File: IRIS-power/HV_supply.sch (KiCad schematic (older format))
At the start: 17 parts

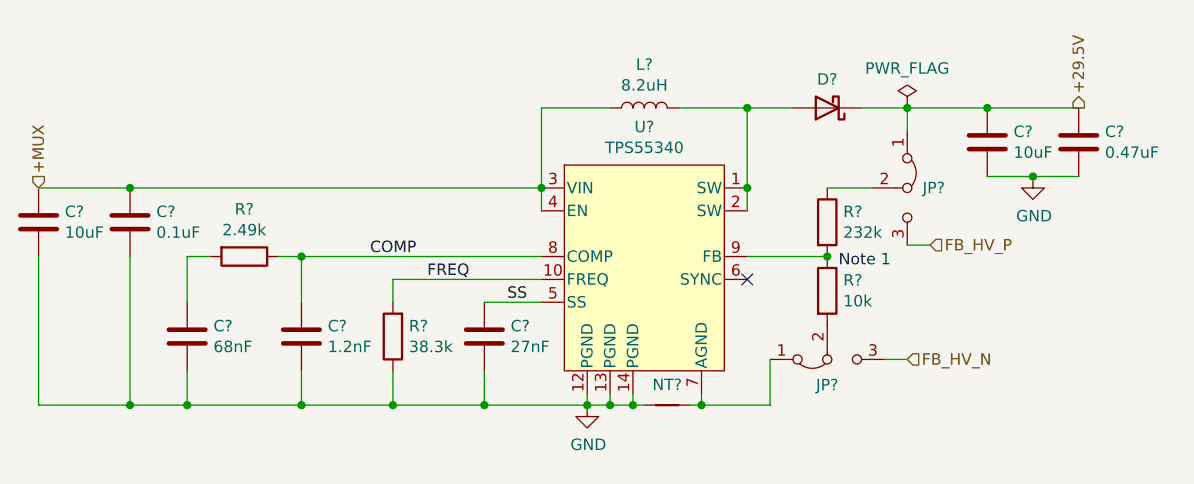
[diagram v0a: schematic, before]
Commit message: Finalized power board V2 schematic, preparing to layout
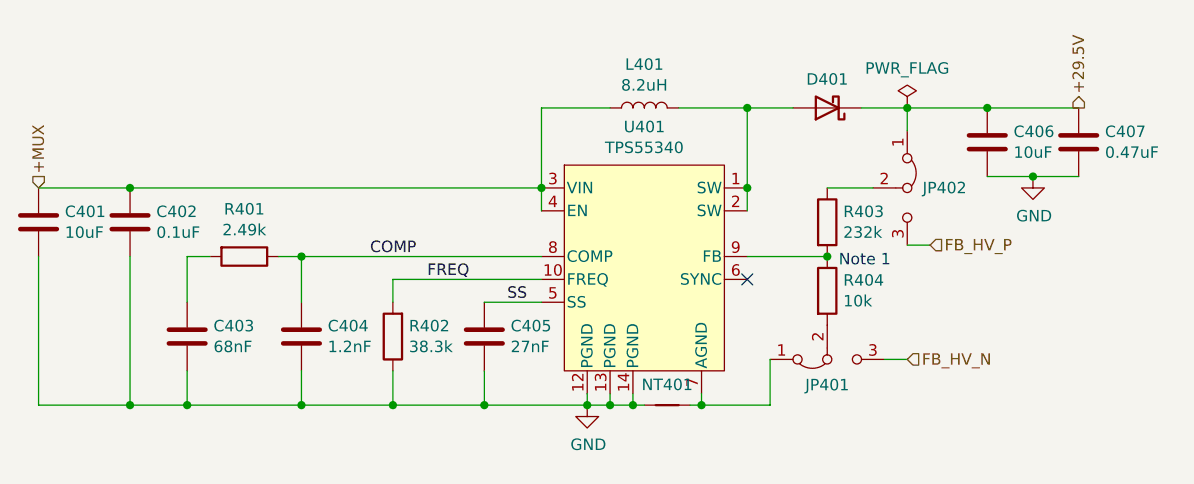
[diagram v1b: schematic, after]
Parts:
- C401, C406: renamed from C?; footprint Capacitor_SMD:C_1206_3216Metric -> Capacitor_SMD:C_0603_1608Metric
- C402, C403, C404, C407: renamed from C?; footprint (none) -> Capacitor_SMD:C_0603_1608Metric
- JP401, JP402: renamed from JP?; footprint (none) -> Connector_PinHeader_2.54mm:PinHeader_1x03_P2.54mm_Vertical
- L401: renamed from L?; footprint (none) -> star-common-lib:VLS6045AF
- NT401: renamed from NT?; footprint (none) -> NetTie:NetTie-2_SMD_Pad0.5mm
- R401: renamed from R?; footprint (none) -> Resistor_SMD:R_0603_1608Metric
- U401: renamed from U?; footprint (none) -> star-common-lib:TPS55340
- gave numbers to parts that had none: 5
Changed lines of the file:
@@
 $Descr A4 11693 8268
 encoding utf-8
-Sheet 5 9
+Sheet 4 8
 Title ""
 Date ""
@@
 P 5000 4250
 AR Path="/5F441757" Ref="R?"  Part="1"
-AR Path="/5F41AE09/5F441757" Ref="R?"  Part="1"
-F 0 "R?" H 4930 4204 50  0000 R CNN
+AR Path="/5F41AE09/5F441757" Ref="R402"  Part="1"
+F 0 "R402" H 4930 4204 50  0000 R CNN
 F 1 "38.3k" H 4930 4295 50  0000 R CNN
 F 2 "Resistor_SMD:R_0603_1608Metric" V 4930 4250 50  0001 C CNN
@@
 P 5400 4250
 AR Path="/5F44175D" Ref="C?"  Part="1"
-AR Path="/5F41AE09/5F44175D" Ref="C?"  Part="1"
-F 0 "C?" H 5515 4296 50  0000 L CNN
+AR Path="/5F41AE09/5F44175D" Ref="C405"  Part="1"
+F 0 "C405" H 5515 4296 50  0000 L CNN
 F 1 "27nF" H 5515 4205 50  0000 L CNN
 F 2 "Capacitor_SMD:C_0603_1608Metric" H 5438 4100 50  0001 C CNN
@@
 P 3450 3750
 AR Path="/5F441768" Ref="C?"  Part="1"
-AR Path="/5F41AE09/5F441768" Ref="C?"  Part="1"
-F 0 "C?" H 3565 3796 50  0000 L CNN
+AR Path="/5F41AE09/5F441768" Ref="C401"  Part="1"
+F 0 "C401" H 3565 3796 50  0000 L CNN
 F 1 "10uF" H 3565 3705 50  0000 L CNN
-F 2 "Capacitor_SMD:C_1206_3216Metric" H 3488 3600 50  0001 C CNN
+F 2 "Capacitor_SMD:C_0603_1608Metric" H 3488 3600 50  0001 C CNN
 F 3 "~" H 3450 3750 50  0001 C CNN
 F 4 "X5R, 16V" H 3450 3750 50  0001 C CNN "Notes"
@@
 P 6900 3750
 AR Path="/5F44176E" Ref="R?"  Part="1"
-AR Path="/5F41AE09/5F44176E" Ref="R?"  Part="1"
-F 0 "R?" H 6970 3796 50  0000 L CNN
+AR Path="/5F41AE09/5F44176E" Ref="R403"  Part="1"
+F 0 "R403" H 6970 3796 50  0000 L CNN
 F 1 "232k" H 6970 3705 50  0000 L CNN
 F 2 "Resistor_SMD:R_0603_1608Metric" V 6830 3750 50  0001 C CNN
@@
 P 6900 4050
 AR Path="/5F441774" Ref="R?"  Part="1"
-AR Path="/5F41AE09/5F441774" Ref="R?"  Part="1"
-F 0 "R?" H 6970 4096 50  0000 L CNN
+AR Path="/5F41AE09/5F441774" Ref="R404"  Part="1"
+F 0 "R404" H 6970 4096 50  0000 L CNN
 F 1 "10k" H 6970 4005 50  0000 L CNN
 F 2 "Resistor_SMD:R_0603_1608Metric" V 6830 4050 50  0001 C CNN
@@
 P 7600 3400
 AR Path="/5F44177A" Ref="C?"  Part="1"
-AR Path="/5F41AE09/5F44177A" Ref="C?"  Part="1"
-F 0 "C?" H 7715 3446 50  0000 L CNN
+AR Path="/5F41AE09/5F44177A" Ref="C406"  Part="1"
+F 0 "C406" H 7715 3446 50  0000 L CNN
 F 1 "10uF" H 7715 3355 50  0000 L CNN
-F 2 "Capacitor_SMD:C_1206_3216Metric" H 7638 3250 50  0001 C CNN
+F 2 "Capacitor_SMD:C_0603_1608Metric" H 7638 3250 50  0001 C CNN
 F 3 "1276-3387-1-ND" H 7600 3400 50  0001 C CNN
 	1    7600 3400
@@
 P 5850 4550
 AR Path="/5F441780" Ref="#PWR?"  Part="1"
-AR Path="/5F41AE09/5F441780" Ref="#PWR?"  Part="1"
-F 0 "#PWR?" H 5850 4300 50  0001 C CNN
+AR Path="/5F41AE09/5F441780" Ref="#PWR0401"  Part="1"
+F 0 "#PWR0401" H 5850 4300 50  0001 C CNN
 F 1 "GND" H 5855 4377 50  0000 C CNN
 F 2 "" H 5850 4550 50  0001 C CNN
@@
 P 7250 3250
 AR Path="/5F441786" Ref="#FLG?"  Part="1"
-AR Path="/5F41AE09/5F441786" Ref="#FLG?"  Part="1"
-F 0 "#FLG?" H 7250 3325 50  0001 C CNN
+AR Path="/5F41AE09/5F441786" Ref="#FLG0401"  Part="1"
+F 0 "#FLG0401" H 7250 3325 50  0001 C CNN
 F 1 "PWR_FLAG" H 7250 3423 50  0000 C CNN
 F 2 "" H 7250 3250 50  0001 C CNN
@@
 P 6100 3950
 AR Path="/5F44178F" Ref="U?"  Part="1"
-AR Path="/5F41AE09/5F44178F" Ref="U?"  Part="1"
-F 0 "U?" H 6100 4567 50  0000 C CNN
+AR Path="/5F41AE09/5F44178F" Ref="U401"  Part="1"
+F 0 "U401" H 6100 4567 50  0000 C CNN
 F 1 "TPS55340" H 6100 4476 50  0000 C CNN
-F 2 "" H 6100 3700 50  0001 L CNN
+F 2 "star-common-lib:TPS55340" H 6100 3700 50  0001 L CNN
 F 3 "" H 5850 3600 50  0001 C CNN
 	1    6100 3950
@@
 P 6100 3250
 AR Path="/5F4417A5" Ref="L?"  Part="1"
-AR Path="/5F41AE09/5F4417A5" Ref="L?"  Part="1"
-F 0 "L?" V 6290 3250 50  0000 C CNN
+AR Path="/5F41AE09/5F4417A5" Ref="L401"  Part="1"
+F 0 "L401" V 6290 3250 50  0000 C CNN
 F 1 "8.2uH" V 6199 3250 50  0000 C CNN
-F 2 "" H 6100 3250 50  0001 C CNN
+F 2 "star-common-lib:VLS6045AF" H 6100 3250 50  0001 C CNN
 F 3 "https://product.tdk.com/info/en/catalog/datasheets/inductor_commercial_power_vls6045af_en.pdf" H 6100 3250 50  0001 C CNN
 F 4 "445-VLS6045AF-8R2MCT-ND" H 6100 3250 50  0001 C CNN "Digikey PN"
@@
 P 6900 3250
 AR Path="/5F4417AE" Ref="D?"  Part="1"
-AR Path="/5F41AE09/5F4417AE" Ref="D?"  Part="1"
-F 0 "D?" H 6900 3125 50  0000 C CNN
+AR Path="/5F41AE09/5F4417AE" Ref="D401"  Part="1"
+F 0 "D401" H 6900 3125 50  0000 C CNN
 F 1 "D_Schottky" H 6900 3124 50  0001 C CNN
 F 2 "Diode_SMD:D_SMA_Handsoldering" H 6900 3250 50  0001 C CNN
@@
 P 4100 4250
 AR Path="/5F4417B4" Ref="C?"  Part="1"
-AR Path="/5F41AE09/5F4417B4" Ref="C?"  Part="1"
-F 0 "C?" H 4215 4296 50  0000 L CNN
+AR Path="/5F41AE09/5F4417B4" Ref="C403"  Part="1"
+F 0 "C403" H 4215 4296 50  0000 L CNN
 F 1 "68nF" H 4215 4205 50  0000 L CNN
-F 2 "" H 4138 4100 50  0001 C CNN
+F 2 "Capacitor_SMD:C_0603_1608Metric" H 4138 4100 50  0001 C CNN
 F 3 "~" H 4100 4250 50  0001 C CNN
 	1    4100 4250
@@
 P 4600 4250
 AR Path="/5F4417BA" Ref="C?"  Part="1"
-AR Path="/5F41AE09/5F4417BA" Ref="C?"  Part="1"
-F 0 "C?" H 4715 4296 50  0000 L CNN
+AR Path="/5F41AE09/5F4417BA" Ref="C404"  Part="1"
+F 0 "C404" H 4715 4296 50  0000 L CNN
 F 1 "1.2nF" H 4715 4205 50  0000 L CNN
-F 2 "" H 4638 4100 50  0001 C CNN
+F 2 "Capacitor_SMD:C_0603_1608Metric" H 4638 4100 50  0001 C CNN
 F 3 "~" H 4600 4250 50  0001 C CNN
 	1    4600 4250
@@
 P 4350 3900
 AR Path="/5F4417C0" Ref="R?"  Part="1"
-AR Path="/5F41AE09/5F4417C0" Ref="R?"  Part="1"
-F 0 "R?" V 4143 3900 50  0000 C CNN
+AR Path="/5F41AE09/5F4417C0" Ref="R401"  Part="1"
+F 0 "R401" V 4143 3900 50  0000 C CNN
 F 1 "2.49k" V 4234 3900 50  0000 C CNN
-F 2 "" V 4280 3900 50  0001 C CNN
+F 2 "Resistor_SMD:R_0603_1608Metric" V 4280 3900 50  0001 C CNN
 F 3 "~" H 4350 3900 50  0001 C CNN
 	1    4350 3900
@@
 P 7250 3600
 AR Path="/5F4417C6" Ref="JP?"  Part="1"
-AR Path="/5F41AE09/5F4417C6" Ref="JP?"  Part="1"
-F 0 "JP?" V 7250 3667 50  0000 L CNN
+AR Path="/5F41AE09/5F4417C6" Ref="JP402"  Part="1"
+F 0 "JP402" V 7250 3667 50  0000 L CNN
 F 1 "Jumper_3_Bridged12" V 7295 3667 50  0001 L CNN
-F 2 "" H 7250 3600 50  0001 C CNN
+F 2 "Connector_PinHeader_2.54mm:PinHeader_1x03_P2.54mm_Vertical" H 7250 3600 50  0001 C CNN
 F 3 "~" H 7250 3600 50  0001 C CNN
 	1    7250 3600
@@
 P 6900 4350
 AR Path="/5F4417CE" Ref="JP?"  Part="1"
-AR Path="/5F41AE09/5F4417CE" Ref="JP?"  Part="1"
-F 0 "JP?" H 6900 4462 50  0000 C CNN
+AR Path="/5F41AE09/5F4417CE" Ref="JP401"  Part="1"
+F 0 "JP401" H 6900 4462 50  0000 C CNN
 F 1 "Jumper_3_Bridged12" H 6900 4552 50  0001 C CNN
-F 2 "" H 6900 4350 50  0001 C CNN
+F 2 "Connector_PinHeader_2.54mm:PinHeader_1x03_P2.54mm_Vertical" H 6900 4350 50  0001 C CNN
 F 3 "~" H 6900 4350 50  0001 C CNN
 	1    6900 4350
@@
 P 6200 4550
 AR Path="/5F4417D4" Ref="NT?"  Part="1"
-AR Path="/5F41AE09/5F4417D4" Ref="NT?"  Part="1"
-F 0 "NT?" H 6200 4639 50  0000 C CNN
+AR Path="/5F41AE09/5F4417D4" Ref="NT401"  Part="1"
+F 0 "NT401" H 6200 4639 50  0000 C CNN
 F 1 "Net-Tie_2" H 6200 4640 50  0001 C CNN
-F 2 "" H 6200 4550 50  0001 C CNN
+F 2 "NetTie:NetTie-2_SMD_Pad0.5mm" H 6200 4550 50  0001 C CNN
 F 3 "~" H 6200 4550 50  0001 C CNN
 	1    6200 4550
@@
 P 7800 3550
 AR Path="/5F4417FB" Ref="#PWR?"  Part="1"
-AR Path="/5F41AE09/5F4417FB" Ref="#PWR?"  Part="1"
-F 0 "#PWR?" H 7800 3300 50  0001 C CNN
+AR Path="/5F41AE09/5F4417FB" Ref="#PWR0402"  Part="1"
+F 0 "#PWR0402" H 7800 3300 50  0001 C CNN
 F 1 "GND" H 7805 3377 50  0000 C CNN
 F 2 "" H 7800 3550 50  0001 C CNN
@@
 P 3850 3750
 AR Path="/5F44180C" Ref="C?"  Part="1"
-AR Path="/5F41AE09/5F44180C" Ref="C?"  Part="1"
-F 0 "C?" H 3965 3796 50  0000 L CNN
+AR Path="/5F41AE09/5F44180C" Ref="C402"  Part="1"
+F 0 "C402" H 3965 3796 50  0000 L CNN
 F 1 "0.1uF" H 3965 3705 50  0000 L CNN
-F 2 "" H 3888 3600 50  0001 C CNN
+F 2 "Capacitor_SMD:C_0603_1608Metric" H 3888 3600 50  0001 C CNN
 F 3 "~" H 3850 3750 50  0001 C CNN
 	1    3850 3750
@@
 P 8000 3400
 AR Path="/5F441812" Ref="C?"  Part="1"
-AR Path="/5F41AE09/5F441812" Ref="C?"  Part="1"
-F 0 "C?" H 8115 3446 50  0000 L CNN
+AR Path="/5F41AE09/5F441812" Ref="C407"  Part="1"
+F 0 "C407" H 8115 3446 50  0000 L CNN
 F 1 "0.47uF" H 8115 3355 50  0000 L CNN
-F 2 "" H 8038 3250 50  0001 C CNN
+F 2 "Capacitor_SMD:C_0603_1608Metric" H 8038 3250 50  0001 C CNN
 F 3 "~" H 8000 3400 50  0001 C CNN
 	1    8000 3400

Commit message: Updated layout
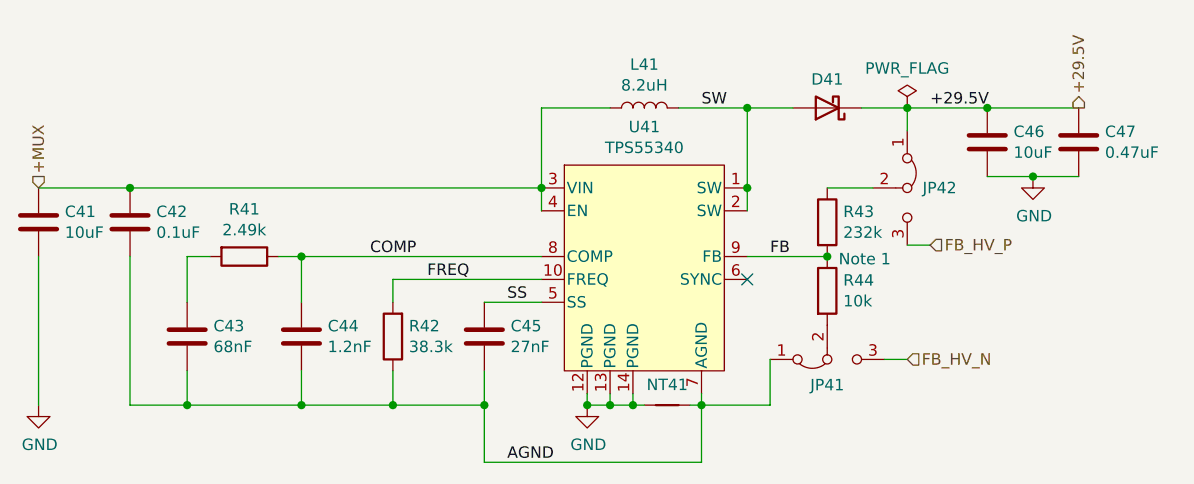
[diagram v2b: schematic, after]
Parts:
- C46: renamed from C406; footprint Capacitor_SMD:C_0603_1608Metric -> Capacitor_SMD:C_0805_2012Metric
- renumbered C401 to C41, C402 to C42, C403 to C43, C404 to C44, C405 to C45, C407 to C47, D401 to D41, JP401 to JP41, JP402 to JP42, L401 to L41, NT401 to NT41, R401 to R41, R402 to R42, R403 to R43, R404 to R44, U401 to U41
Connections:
- net GND: no longer C42.2, C43.2, C44.2, C45.2, R42.1
- net FB: now reaches R43.2, R44.1, U41.9 (FB)
- net SW: now reaches D41.2 (A), L41.2, U41.1 (SW), U41.2 (SW)
- net AGND: now reaches JP41.1 (A), NT41.2, U41.7 (AGND)
- net AGND: now also C42.2, C43.2, C44.2, C45.2, R42.1
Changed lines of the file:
@@
 	6550 3600 6550 3700
 Connection ~ 6550 3600
-Connection ~ 5400 4550
-Wire Wire Line
-	5400 4550 5850 4550
 Connection ~ 5650 3600
 Connection ~ 3850 3600
@@
 P 5000 4250
 AR Path="/5F441757" Ref="R?"  Part="1"
-AR Path="/5F41AE09/5F441757" Ref="R402"  Part="1"
-F 0 "R402" H 4930 4204 50  0000 R CNN
+AR Path="/5F41AE09/5F441757" Ref="R42"  Part="1"
+F 0 "R42" H 4930 4204 50  0000 R CNN
 F 1 "38.3k" H 4930 4295 50  0000 R CNN
 F 2 "Resistor_SMD:R_0603_1608Metric" V 4930 4250 50  0001 C CNN
@@
 P 5400 4250
 AR Path="/5F44175D" Ref="C?"  Part="1"
-AR Path="/5F41AE09/5F44175D" Ref="C405"  Part="1"
-F 0 "C405" H 5515 4296 50  0000 L CNN
+AR Path="/5F41AE09/5F44175D" Ref="C45"  Part="1"
+F 0 "C45" H 5515 4296 50  0000 L CNN
 F 1 "27nF" H 5515 4205 50  0000 L CNN
 F 2 "Capacitor_SMD:C_0603_1608Metric" H 5438 4100 50  0001 C CNN
@@
 P 3450 3750
 AR Path="/5F441768" Ref="C?"  Part="1"
-AR Path="/5F41AE09/5F441768" Ref="C401"  Part="1"
-F 0 "C401" H 3565 3796 50  0000 L CNN
+AR Path="/5F41AE09/5F441768" Ref="C41"  Part="1"
+F 0 "C41" H 3565 3796 50  0000 L CNN
 F 1 "10uF" H 3565 3705 50  0000 L CNN
 F 2 "Capacitor_SMD:C_0603_1608Metric" H 3488 3600 50  0001 C CNN
@@
 P 6900 3750
 AR Path="/5F44176E" Ref="R?"  Part="1"
-AR Path="/5F41AE09/5F44176E" Ref="R403"  Part="1"
-F 0 "R403" H 6970 3796 50  0000 L CNN
+AR Path="/5F41AE09/5F44176E" Ref="R43"  Part="1"
+F 0 "R43" H 6970 3796 50  0000 L CNN
 F 1 "232k" H 6970 3705 50  0000 L CNN
 F 2 "Resistor_SMD:R_0603_1608Metric" V 6830 3750 50  0001 C CNN
@@
 P 6900 4050
 AR Path="/5F441774" Ref="R?"  Part="1"
-AR Path="/5F41AE09/5F441774" Ref="R404"  Part="1"
-F 0 "R404" H 6970 4096 50  0000 L CNN
+AR Path="/5F41AE09/5F441774" Ref="R44"  Part="1"
+F 0 "R44" H 6970 4096 50  0000 L CNN
 F 1 "10k" H 6970 4005 50  0000 L CNN
 F 2 "Resistor_SMD:R_0603_1608Metric" V 6830 4050 50  0001 C CNN
@@
 P 7600 3400
 AR Path="/5F44177A" Ref="C?"  Part="1"
-AR Path="/5F41AE09/5F44177A" Ref="C406"  Part="1"
-F 0 "C406" H 7715 3446 50  0000 L CNN
+AR Path="/5F41AE09/5F44177A" Ref="C46"  Part="1"
+F 0 "C46" H 7715 3446 50  0000 L CNN
 F 1 "10uF" H 7715 3355 50  0000 L CNN
-F 2 "Capacitor_SMD:C_0603_1608Metric" H 7638 3250 50  0001 C CNN
+F 2 "Capacitor_SMD:C_0805_2012Metric" H 7638 3250 50  0001 C CNN
 F 3 "1276-3387-1-ND" H 7600 3400 50  0001 C CNN
 	1    7600 3400
@@
 P 5850 4550
 AR Path="/5F441780" Ref="#PWR?"  Part="1"
-AR Path="/5F41AE09/5F441780" Ref="#PWR0401"  Part="1"
-F 0 "#PWR0401" H 5850 4300 50  0001 C CNN
+AR Path="/5F41AE09/5F441780" Ref="#PWR042"  Part="1"
+F 0 "#PWR042" H 5850 4300 50  0001 C CNN
 F 1 "GND" H 5855 4377 50  0000 C CNN
 F 2 "" H 5850 4550 50  0001 C CNN
@@
 P 7250 3250
 AR Path="/5F441786" Ref="#FLG?"  Part="1"
-AR Path="/5F41AE09/5F441786" Ref="#FLG0401"  Part="1"
-F 0 "#FLG0401" H 7250 3325 50  0001 C CNN
+AR Path="/5F41AE09/5F441786" Ref="#FLG041"  Part="1"
+F 0 "#FLG041" H 7250 3325 50  0001 C CNN
 F 1 "PWR_FLAG" H 7250 3423 50  0000 C CNN
 F 2 "" H 7250 3250 50  0001 C CNN
@@
 P 6100 3950
 AR Path="/5F44178F" Ref="U?"  Part="1"
-AR Path="/5F41AE09/5F44178F" Ref="U401"  Part="1"
-F 0 "U401" H 6100 4567 50  0000 C CNN
+AR Path="/5F41AE09/5F44178F" Ref="U41"  Part="1"
+F 0 "U41" H 6100 4567 50  0000 C CNN
 F 1 "TPS55340" H 6100 4476 50  0000 C CNN
 F 2 "star-common-lib:TPS55340" H 6100 3700 50  0001 L CNN
@@
 P 6100 3250
 AR Path="/5F4417A5" Ref="L?"  Part="1"
-AR Path="/5F41AE09/5F4417A5" Ref="L401"  Part="1"
-F 0 "L401" V 6290 3250 50  0000 C CNN
+AR Path="/5F41AE09/5F4417A5" Ref="L41"  Part="1"
+F 0 "L41" V 6290 3250 50  0000 C CNN
 F 1 "8.2uH" V 6199 3250 50  0000 C CNN
 F 2 "star-common-lib:VLS6045AF" H 6100 3250 50  0001 C CNN
@@
 P 6900 3250
 AR Path="/5F4417AE" Ref="D?"  Part="1"
-AR Path="/5F41AE09/5F4417AE" Ref="D401"  Part="1"
-F 0 "D401" H 6900 3125 50  0000 C CNN
+AR Path="/5F41AE09/5F4417AE" Ref="D41"  Part="1"
+F 0 "D41" H 6900 3125 50  0000 C CNN
 F 1 "D_Schottky" H 6900 3124 50  0001 C CNN
 F 2 "Diode_SMD:D_SMA_Handsoldering" H 6900 3250 50  0001 C CNN
@@
 P 4100 4250
 AR Path="/5F4417B4" Ref="C?"  Part="1"
-AR Path="/5F41AE09/5F4417B4" Ref="C403"  Part="1"
-F 0 "C403" H 4215 4296 50  0000 L CNN
+AR Path="/5F41AE09/5F4417B4" Ref="C43"  Part="1"
+F 0 "C43" H 4215 4296 50  0000 L CNN
 F 1 "68nF" H 4215 4205 50  0000 L CNN
 F 2 "Capacitor_SMD:C_0603_1608Metric" H 4138 4100 50  0001 C CNN
@@
 P 4600 4250
 AR Path="/5F4417BA" Ref="C?"  Part="1"
-AR Path="/5F41AE09/5F4417BA" Ref="C404"  Part="1"
-F 0 "C404" H 4715 4296 50  0000 L CNN
+AR Path="/5F41AE09/5F4417BA" Ref="C44"  Part="1"
+F 0 "C44" H 4715 4296 50  0000 L CNN
 F 1 "1.2nF" H 4715 4205 50  0000 L CNN
 F 2 "Capacitor_SMD:C_0603_1608Metric" H 4638 4100 50  0001 C CNN
@@
 P 4350 3900
 AR Path="/5F4417C0" Ref="R?"  Part="1"
-AR Path="/5F41AE09/5F4417C0" Ref="R401"  Part="1"
-F 0 "R401" V 4143 3900 50  0000 C CNN
+AR Path="/5F41AE09/5F4417C0" Ref="R41"  Part="1"
+F 0 "R41" V 4143 3900 50  0000 C CNN
 F 1 "2.49k" V 4234 3900 50  0000 C CNN
 F 2 "Resistor_SMD:R_0603_1608Metric" V 4280 3900 50  0001 C CNN
@@
 P 7250 3600
 AR Path="/5F4417C6" Ref="JP?"  Part="1"
-AR Path="/5F41AE09/5F4417C6" Ref="JP402"  Part="1"
-F 0 "JP402" V 7250 3667 50  0000 L CNN
+AR Path="/5F41AE09/5F4417C6" Ref="JP42"  Part="1"
+F 0 "JP42" V 7250 3667 50  0000 L CNN
 F 1 "Jumper_3_Bridged12" V 7295 3667 50  0001 L CNN
 F 2 "Connector_PinHeader_2.54mm:PinHeader_1x03_P2.54mm_Vertical" H 7250 3600 50  0001 C CNN
@@
 P 6900 4350
 AR Path="/5F4417CE" Ref="JP?"  Part="1"
-AR Path="/5F41AE09/5F4417CE" Ref="JP401"  Part="1"
-F 0 "JP401" H 6900 4462 50  0000 C CNN
+AR Path="/5F41AE09/5F4417CE" Ref="JP41"  Part="1"
+F 0 "JP41" H 6900 4462 50  0000 C CNN
 F 1 "Jumper_3_Bridged12" H 6900 4552 50  0001 C CNN
 F 2 "Connector_PinHeader_2.54mm:PinHeader_1x03_P2.54mm_Vertical" H 6900 4350 50  0001 C CNN
@@
 P 6200 4550
 AR Path="/5F4417D4" Ref="NT?"  Part="1"
-AR Path="/5F41AE09/5F4417D4" Ref="NT401"  Part="1"
-F 0 "NT401" H 6200 4639 50  0000 C CNN
+AR Path="/5F41AE09/5F4417D4" Ref="NT41"  Part="1"
+F 0 "NT41" H 6200 4639 50  0000 C CNN
 F 1 "Net-Tie_2" H 6200 4640 50  0001 C CNN
 F 2 "NetTie:NetTie-2_SMD_Pad0.5mm" H 6200 4550 50  0001 C CNN
@@
 Wire Wire Line
 	6100 4550 6050 4550
-Connection ~ 3850 4550
-Wire Wire Line
-	3850 4550 3450 4550
-Connection ~ 4100 4550
-Wire Wire Line
-	4100 4550 3850 4550
 Connection ~ 4600 4550
 Wire Wire Line
@@
 P 7800 3550
 AR Path="/5F4417FB" Ref="#PWR?"  Part="1"
-AR Path="/5F41AE09/5F4417FB" Ref="#PWR0402"  Part="1"
-F 0 "#PWR0402" H 7800 3300 50  0001 C CNN
+AR Path="/5F41AE09/5F4417FB" Ref="#PWR043"  Part="1"
+F 0 "#PWR043" H 7800 3300 50  0001 C CNN
 F 1 "GND" H 7805 3377 50  0000 C CNN
 F 2 "" H 7800 3550 50  0001 C CNN
@@
 P 3850 3750
 AR Path="/5F44180C" Ref="C?"  Part="1"
-AR Path="/5F41AE09/5F44180C" Ref="C402"  Part="1"
-F 0 "C402" H 3965 3796 50  0000 L CNN
+AR Path="/5F41AE09/5F44180C" Ref="C42"  Part="1"
+F 0 "C42" H 3965 3796 50  0000 L CNN
 F 1 "0.1uF" H 3965 3705 50  0000 L CNN
 F 2 "Capacitor_SMD:C_0603_1608Metric" H 3888 3600 50  0001 C CNN
@@
 P 8000 3400
 AR Path="/5F441812" Ref="C?"  Part="1"
-AR Path="/5F41AE09/5F441812" Ref="C407"  Part="1"
-F 0 "C407" H 8115 3446 50  0000 L CNN
+AR Path="/5F41AE09/5F441812" Ref="C47"  Part="1"
+F 0 "C47" H 8115 3446 50  0000 L CNN
 F 1 "0.47uF" H 8115 3355 50  0000 L CNN
 F 2 "Capacitor_SMD:C_0603_1608Metric" H 8038 3250 50  0001 C CNN
@@
 Wire Wire Line
 	7350 3850 7250 3850
+$Comp
+L power:GND #PWR?
+U 1 1 5F30F5B2
+P 3450 4550
+AR Path="/5F30F5B2" Ref="#PWR?"  Part="1"
+AR Path="/5F41AE09/5F30F5B2" Ref="#PWR041"  Part="1"
+F 0 "#PWR041" H 3450 4300 50  0001 C CNN
+F 1 "GND" H 3455 4377 50  0000 C CNN
+F 2 "" H 3450 4550 50  0001 C CNN
+F 3 "" H 3450 4550 50  0001 C CNN
+	1    3450 4550
+	1    0    0    -1
+$EndComp
+Wire Wire Line
+	5400 4550 5400 4800
+Wire Wire Line
+	5400 4800 6350 4800
+Wire Wire Line
+	6350 4800 6350 4550
+Connection ~ 5400 4550
+Wire Wire Line
+	3850 4550 4100 4550
+Connection ~ 4100 4550
+Text Label 5500 4800 0    50   ~ 0
+AGND
+Text Label 6650 3900 0    50   ~ 0
+FB
+Text Label 6350 3250 0    50   ~ 0
+SW
+Text Label 7350 3250 0    50   ~ 0
++29.5V
 $EndSCHEMATC

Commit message: Added some 3D models
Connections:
- net AGND: now also NT41.1; no longer NT41.2, U41.7 (AGND)
- net GND: now also NT41.2, U41.7 (AGND); no longer NT41.1
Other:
- moved on the sheet: NT41
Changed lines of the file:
@@
 	5950 3250 5650 3250
 NoConn ~ 6550 4000
-Connection ~ 6350 4550
-Wire Wire Line
-	6650 4550 6350 4550
 Wire Wire Line
 	6550 3600 6550 3700
@@
 L Device:Net-Tie_2 NT?
 U 1 1 5F4417D4
-P 6200 4550
+P 6350 4650
 AR Path="/5F4417D4" Ref="NT?"  Part="1"
 AR Path="/5F41AE09/5F4417D4" Ref="NT41"  Part="1"
-F 0 "NT41" H 6200 4639 50  0000 C CNN
-F 1 "Net-Tie_2" H 6200 4640 50  0001 C CNN
-F 2 "NetTie:NetTie-2_SMD_Pad0.5mm" H 6200 4550 50  0001 C CNN
-F 3 "~" H 6200 4550 50  0001 C CNN
-	1    6200 4550
-	1    0    0    -1
-$EndComp
-Wire Wire Line
-	6100 4550 6050 4550
+F 0 "NT41" H 6350 4739 50  0000 C CNN
+F 1 "Net-Tie_2" H 6350 4740 50  0001 C CNN
+F 2 "NetTie:NetTie-2_SMD_Pad0.5mm" H 6350 4650 50  0001 C CNN
+F 3 "~" H 6350 4650 50  0001 C CNN
+	1    6350 4650
+	0    -1   -1   0
+$EndComp
 Connection ~ 4600 4550
 Wire Wire Line
@@
 	6050 4550 5950 4550
 Wire Wire Line
-	6300 4550 6350 4550
-Wire Wire Line
 	6350 4550 6350 4500
 Wire Wire Line
 	6550 3900 6900 3900
-Wire Wire Line
-	6650 4350 6650 4550
 Wire Wire Line
 	7250 3350 7250 3250
@@
 Wire Wire Line
 	5400 4800 6350 4800
-Wire Wire Line
-	6350 4800 6350 4550
 Connection ~ 5400 4550
 Wire Wire Line
@@
 Text Label 7350 3250 0    50   ~ 0
 +29.5V
+Wire Wire Line
+	6050 4550 6350 4550
+Connection ~ 6350 4550
+Wire Wire Line
+	6350 4800 6350 4750
+Wire Wire Line
+	6350 4800 6650 4800
+Wire Wire Line
+	6650 4350 6650 4800
+Connection ~ 6350 4800
 $EndSCHEMATC
